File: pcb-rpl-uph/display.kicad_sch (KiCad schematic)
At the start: 1 part, among them J15 20879-040E-01

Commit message: add display connector
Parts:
- added C1 (x5), C5 (x5): 100 nF, local:C_0201_0603Metric, symbol Device:C
- added R1: 150, local:R_0201_0603Metric, symbol Device:R
- added R3: 0, local:R_0201_0603Metric, symbol Device:R
- added R4: 100 k, local:R_0201_0603Metric, symbol Device:R
- added U5: RPL_UPH_FCBGA1744, local:RPL_UPH_FCBGA1744, symbol local:RPL_UPH_FCBGA1744
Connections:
- net GND: now also R1.2, R4.2
- net DC-0: now reaches J15.10 (DP0-)
- net DC-0: now also C1.2
- net DC+1: now reaches J15.12 (DP1+)
- net DC+1: now also C5.2
- net DC-1: now reaches J15.13 (DP1-)
- net DC-1: now also C1.2
- net DC+2: now reaches J15.15 (DP2+)
- net DC+2: now also C5.2
- net DC-2: now reaches J15.16 (DP2-)
- net DC-2: now also C1.2
- net DC+3: now reaches J15.18 (DP3+)
- net DC+3: now also C5.2
- net DC-3: now reaches J15.19 (DP3-)
- net DC-3: now also C1.2
- net HPD_R: now reaches J15.21 (HPD)
- net HPD_R: now also R3.2, R4.1
- net at J15.22 (BACKLIGHT_PWM): now also U5.EL21 (eDP_BKLTCTL)
- net at J15.23 (~{BACKLIGHT_OFF}): now also U5.EN21 (eDP_BKLTEN)
- net AUXC+: now reaches J15.6 (AUX+)
- net AUXC+: now also C5.2
- net AUXC-: now reaches J15.7 (AUX-)
- net AUXC-: now also C1.2
- net DC+0: now reaches J15.9 (DP0+)
- net DC+0: now also C5.2
- new net AUX+: C5.1, U5.AF3 (DDIA_AUXP)
- new net AUX-: C1.1, U5.AG3 (DDIA_AUXN)
- new net D+0: C5.1, U5.AF1 (DDIA_TXP[0])
- new net D+1: C5.1, U5.AB3 (DDIA_TXP[1])
- new net D+2: C5.1, U5.AA1 (DDIA_TXP[2])
- new net D+3: C5.1, U5.W3 (DDIA_TXP[3])
- new net D-0: C1.1, U5.AD1 (DDIA_TXN[0])
- new net D-1: C1.1, U5.AD3 (DDIA_TXN[1])
- new net D-2: C1.1, U5.AB1 (DDIA_TXN[2])
- new net D-3: C1.1, U5.AA3 (DDIA_TXN[3])
- new net DDIA__RCOMP: R1.1, U5.AJ1 (DDIA_RCOMP)
- new net HPD: R3.1, U5.EV25 (GPP_E14/DDSP_HPDA/DISP_MISC_A)
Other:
- note added: "TODO: backlight PWM, enable buffering? 3.3 V power enable, VDDEN on CPU, find pin connect USB, I2C for touchpanel? VBAT switching and protection"
- moved on the sheet: J15

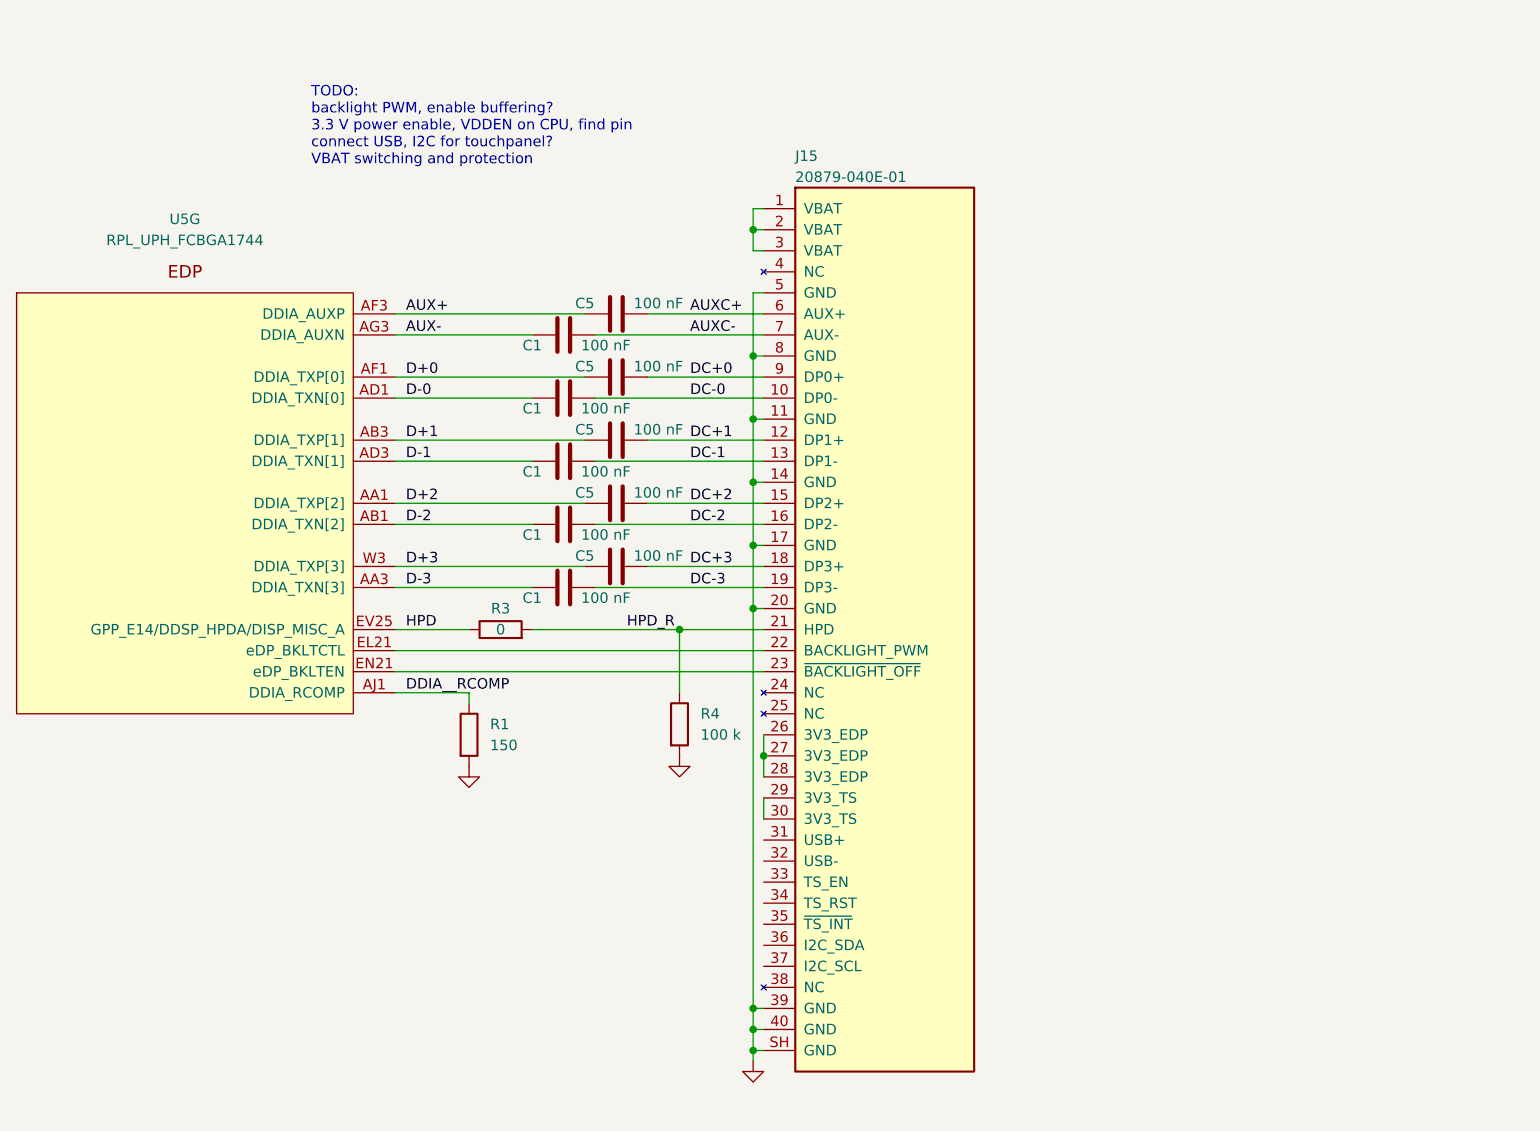
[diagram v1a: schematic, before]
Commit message: refactor much of CPU schematic symbol
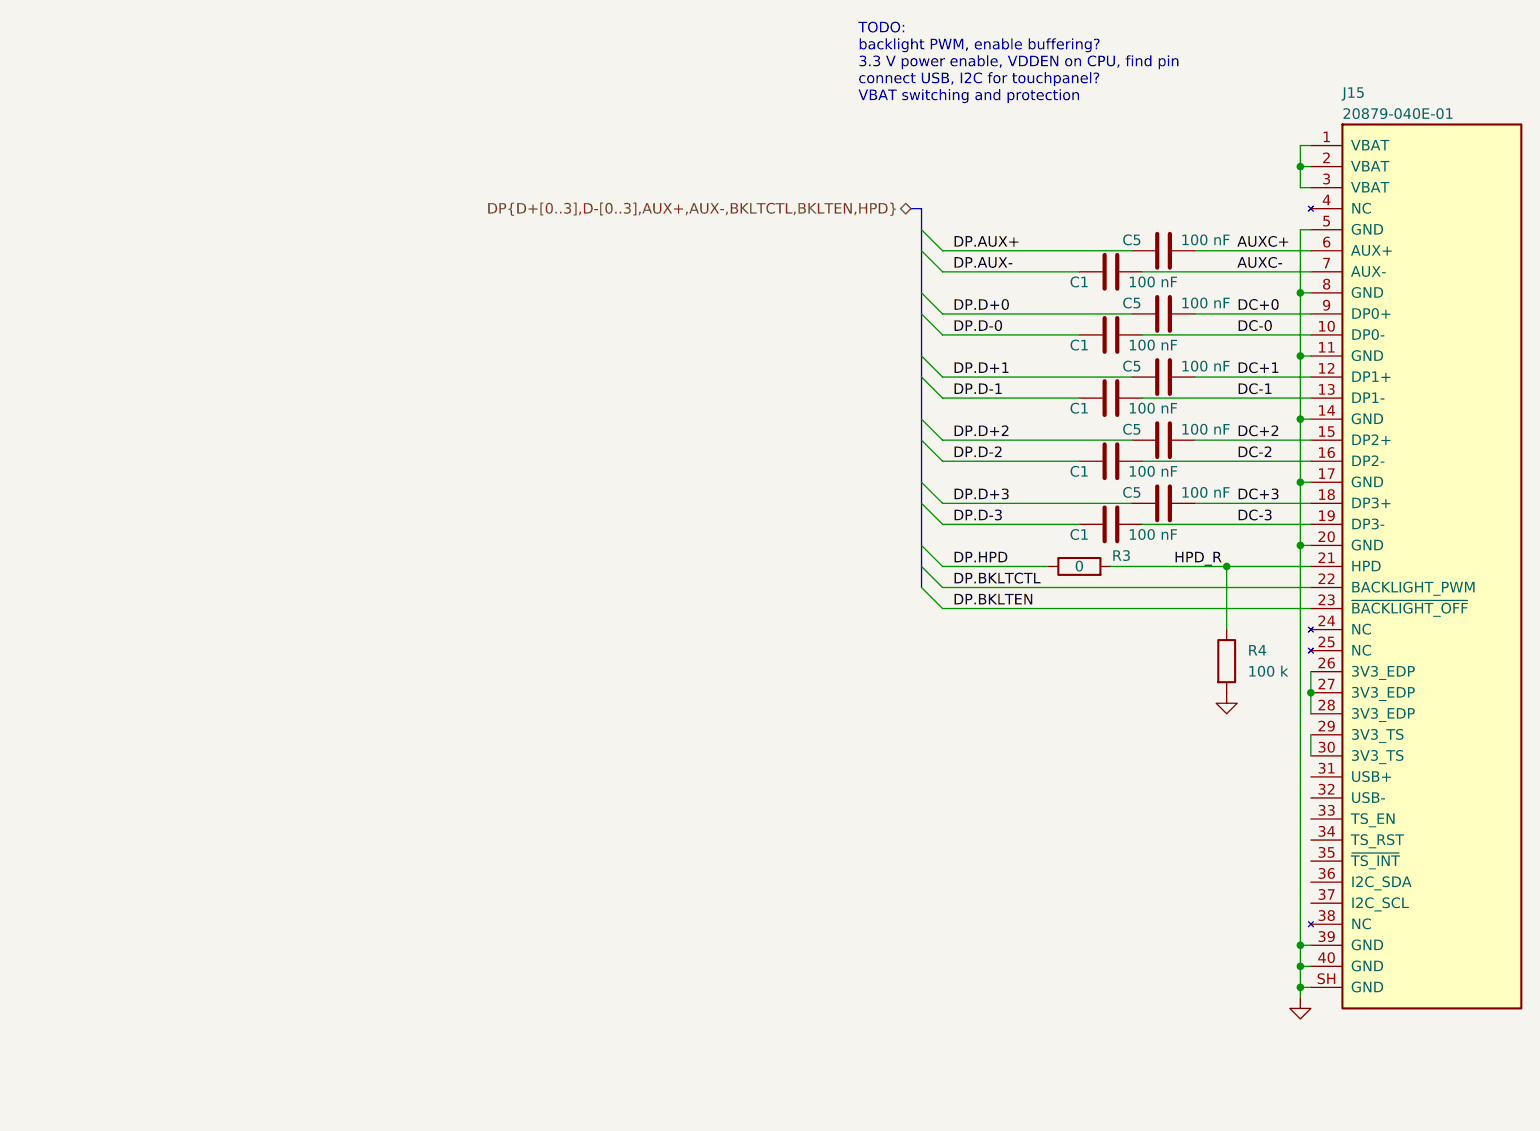
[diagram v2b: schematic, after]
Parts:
- removed R1: 150, local:R_0201_0603Metric, symbol Device:R
- removed U5: RPL_UPH_FCBGA1744, local:RPL_UPH_FCBGA1744, symbol local:RPL_UPH_FCBGA1744
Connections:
- net DP.BKLTCTL: now reaches J15.22 (BACKLIGHT_PWM)
- net DP.BKLTEN: now reaches J15.23 (~{BACKLIGHT_OFF})
- net AUX+ renamed DP.AUX+
- net AUX- renamed DP.AUX-
- net D+0 renamed DP.D+0
- net D+1 renamed DP.D+1
- net D+2 renamed DP.D+2
- net D+3 renamed DP.D+3
- net D-0 renamed DP.D-0
- net D-1 renamed DP.D-1
- net D-2 renamed DP.D-2
- net D-3 renamed DP.D-3
- net HPD renamed DP.HPD
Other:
- moved on the sheet: C1, C5, J15, R3, R4
